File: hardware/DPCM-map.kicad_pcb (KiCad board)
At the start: 2 copper layers, 178 x 178 mm, 106 parts, among them J1 JMP, J10 Conn_01x03_Female, J2 Conn_01x06_Male, J3 Touch_Pad_+, J4 Touch_Pad_0, J5 Touch_Pad_-, J6 JMP, J7 Conn_01x06_Female, J8 Conn_01x03_Female, J9 Conn_01x03_Female, P1 USB_C_Plug, Q1 2N7002, Q2 2N7002, SW1 SW_Push, SW2 SW_+_Fb, SW3 SW_0_Fb, SW4 SW_-_Fb, U1 AZ1117-3.3, U2 BME280, U4 ESP32-WROOM-32, U5 CH340G, Y1 12MHz

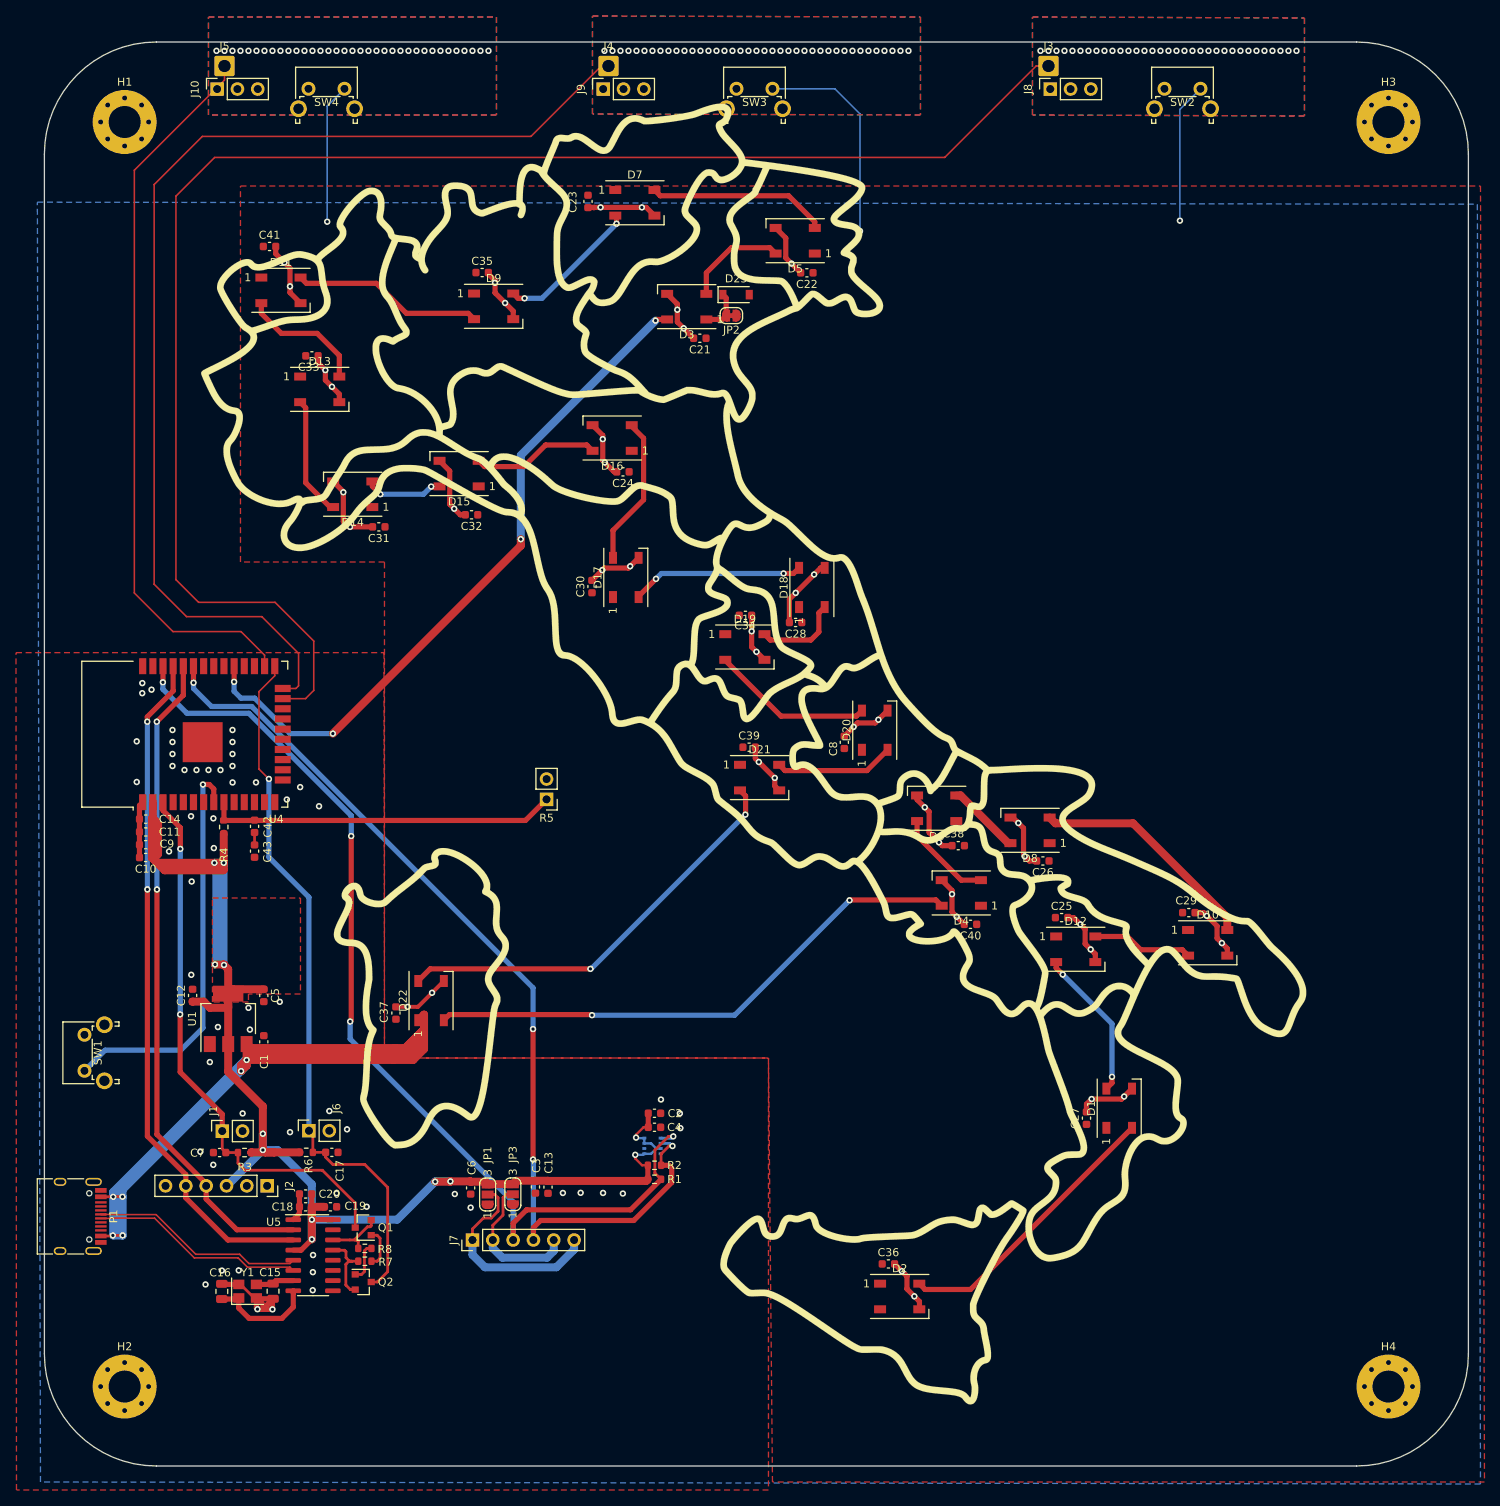
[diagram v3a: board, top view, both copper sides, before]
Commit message: route ws2813 mini and export
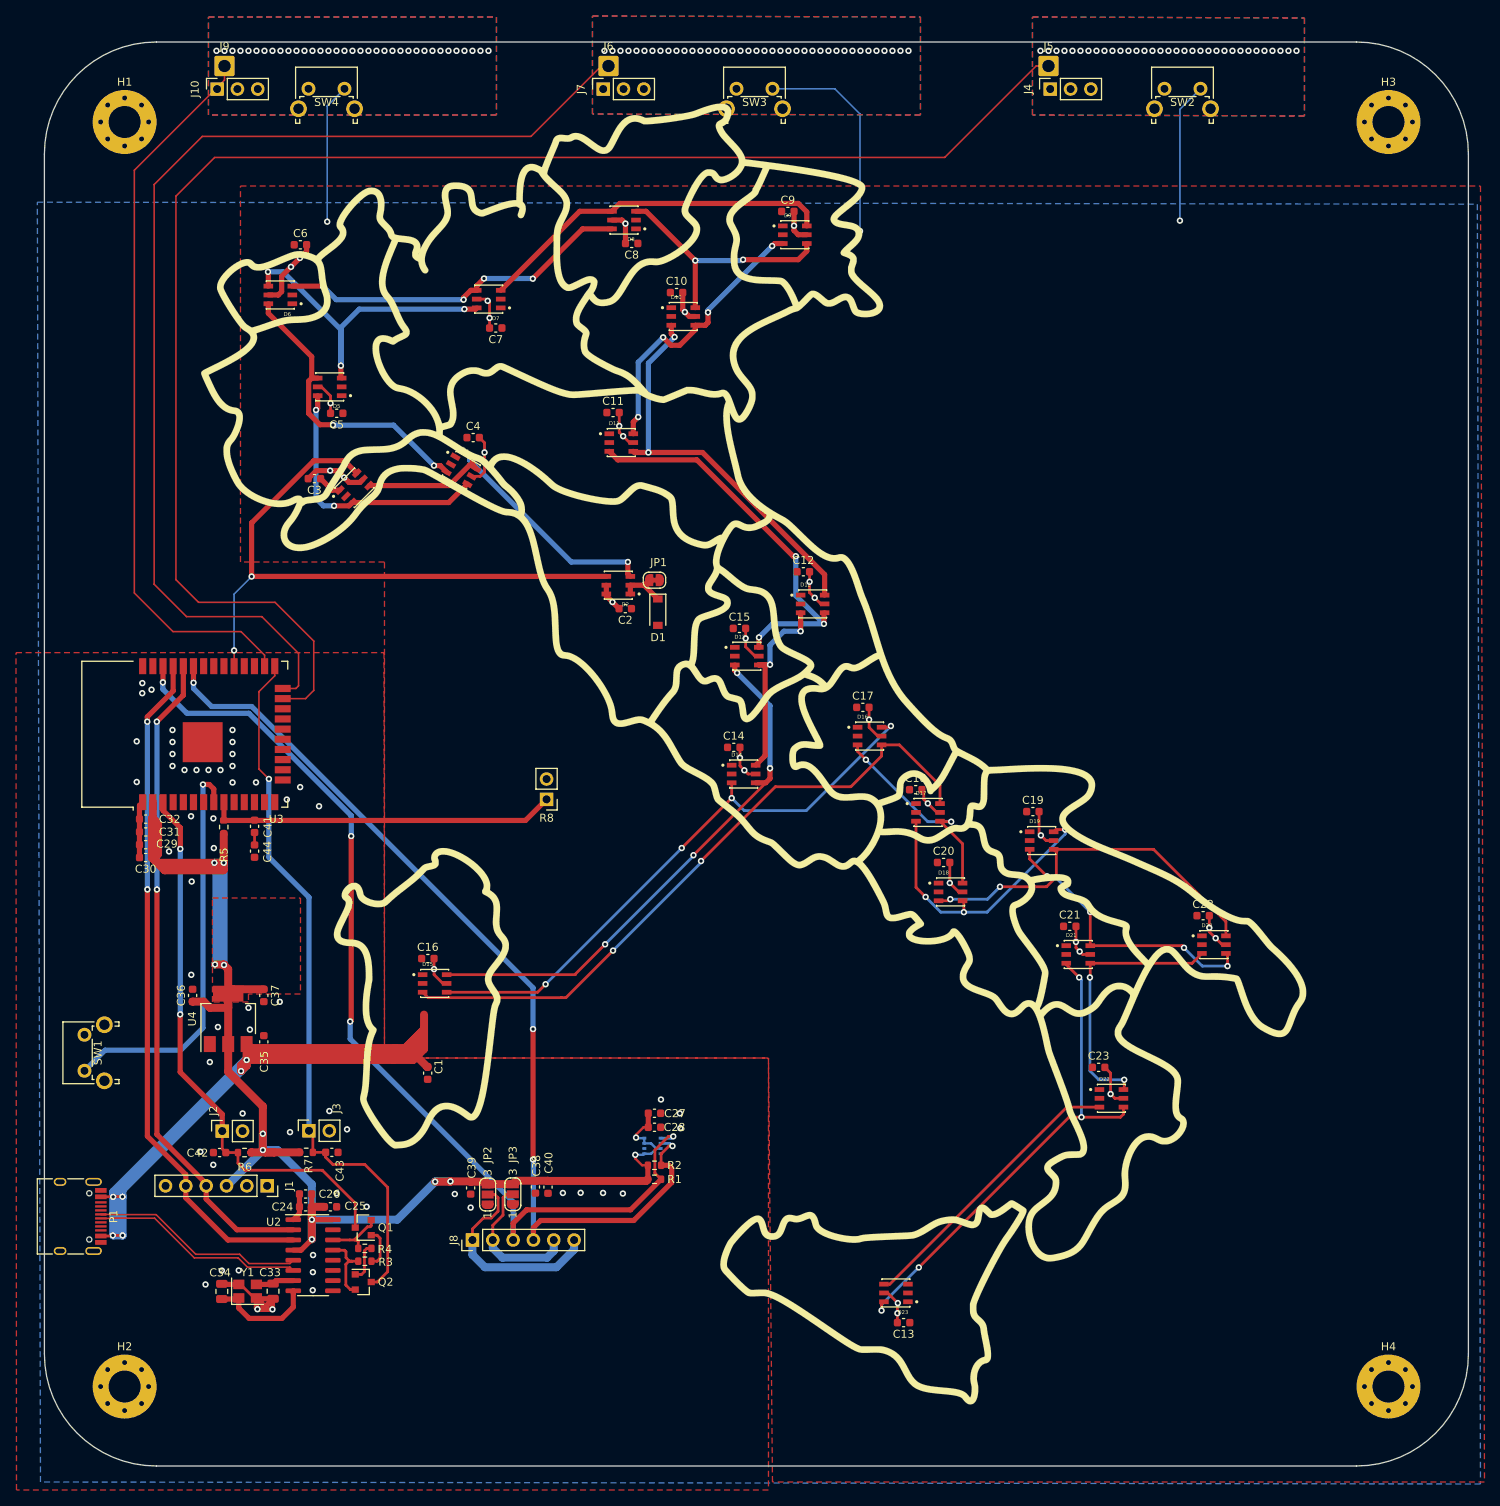
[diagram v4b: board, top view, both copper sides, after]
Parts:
- removed the C24 at (182.8, 103.7)
- removed the C25 at (237.6, 159.4)
- removed the C26 at (235.3, 152.4)
- removed the C27 at (240.8, 184.5)
- removed the C28 at (204.4, 122.6)
- removed the C29 at (253.5, 158.8)
- removed the C30 at (178.9, 118.1)
- removed the C31 at (152.3, 110.6)
- removed the C32 at (163.9, 109.1)
- removed the C33 at (143.9, 89.2)
- removed the C34 at (198.1, 121.7)
- removed the C35 at (165.2, 78.8)
- removed the C36 at (216.0, 202.7)
- removed the C37 at (154.4, 171.4)
- removed the C38 at (224.7, 150.5)
- removed the C39 at (198.6, 138.2)
- removed the C40 at (226.2, 160.3)
- removed the C41 at (138.6, 75.6)
- removed the JP2 at (196.4, 84.2)
- added C1: 10u, Capacitor_SMD:C_0603_1608Metric, F.Cu at (158.4, 178.9)
- added C10: 100n, Capacitor_SMD:C_0603_1608Metric, F.Cu at (189.5, 81.3)
- added C11: 100n, Capacitor_SMD:C_0603_1608Metric, F.Cu at (181.6, 96.3)
- added C12: 100n, Capacitor_SMD:C_0603_1608Metric, F.Cu at (205.4, 116.2)
- added C13: 100n, Capacitor_SMD:C_0603_1608Metric, F.Cu at (217.9, 210.1)
- added C14: 100n, Capacitor_SMD:C_0603_1608Metric, F.Cu at (196.7, 138.2)
- added C15: 100n, Capacitor_SMD:C_0603_1608Metric, F.Cu at (197.4, 123.3)
- added C16: 100n, Capacitor_SMD:C_0603_1608Metric, F.Cu at (158.4, 164.6)
- added C17: 100n, Capacitor_SMD:C_0603_1608Metric, F.Cu at (212.8, 133.2)
- added C18: 100n, Capacitor_SMD:C_0603_1608Metric, F.Cu at (219.4, 143.5)
- added C19: 100n, Capacitor_SMD:C_0603_1608Metric, F.Cu at (234.1, 146.2)
- added C2: 100n, Capacitor_SMD:C_0603_1608Metric, F.Cu at (183.1, 120.8)
- added C20: 100n, Capacitor_SMD:C_0603_1608Metric, F.Cu at (222.9, 152.6)
- added C3: 100n, Capacitor_SMD:C_0603_1608Metric, F.Cu at (144.2, 104.6)
- added C4: 100n, Capacitor_SMD:C_0603_1608Metric, F.Cu at (164.1, 99.5)
- added C5: 100n, Capacitor_SMD:C_0603_1608Metric, F.Cu at (147.0, 96.4)
- added C6: 100n, Capacitor_SMD:C_0603_1608Metric, F.Cu at (142.5, 75.3)
- added C7: 100n, Capacitor_SMD:C_0603_1608Metric, F.Cu at (166.9, 85.8)
- added C9: 100n, Capacitor_SMD:C_0603_1608Metric, F.Cu at (203.4, 71.2)
- added JP1: Jumper, Jumper:SolderJumper-2_P1.3mm_Bridged_RoundedPad1.0x1.5mm, F.Cu at (186.8, 117.3)
- C8: value 10u -> 100n
- D1: value WS2812B -> 1N4148W; footprint LED_SMD:LED_WS2812B_PLCC4_5.0x5.0mm_P3.2mm -> Diode_SMD:D_SOD-123
- D10, D11, D12, D13, D14, D15, D16, D17, D18, D19, D2, D20, D21, D22, D3, D4, D5, D6, D7, D8, D9: value WS2812B -> WS2813; footprint LED_SMD:LED_WS2812B_PLCC4_5.0x5.0mm_P3.2mm -> WS2813MINI:LED_WS2813-MINI
- D23: value 1N4148W -> WS2813; footprint Diode_SMD:D_SOD-123 -> WS2813MINI:LED_WS2813-MINI
- moved D23 126.4 mm to (216.9, 206.4), turned to 180 degrees
- moved C23 125.7 mm to (242.3, 178.2), turned to 0 degrees
- moved D6 104.2 mm to (140.0, 81.6)
- moved D10 102.1 mm to (190.3, 84.3)
- moved D2 95.6 mm to (182.2, 117.9), turned to 180 degrees
- moved C22 94.4 mm to (255.3, 159.2), turned to 0 degrees
- moved D8 91.6 mm to (182.9, 72.3)
- moved C21 86.8 mm to (238.7, 160.5), turned to 0 degrees
- moved D22 85.9 mm to (243.9, 182.0), turned to 0 degrees
- moved D1 84.7 mm to (187.2, 121.3), turned to 270 degrees
- moved D4 81.8 mm to (162.6, 103.5), turned to 330 degrees
- moved C8 67.8 mm to (183.9, 75.2), turned to 180 degrees
- moved D15 63.8 mm to (159.3, 167.7), turned to 0 degrees
- moved D13 62.9 mm to (198.3, 126.8)
- moved D5 61.0 mm to (146.2, 93.1)
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- renumbered C18 to C24, C19 to C25, C20 to C26, C2 to C27, C4 to C28, C9 to C29, C10 to C30, C11 to C31, C14 to C32, C15 to C33, C16 to C34, C1 to C35, C12 to C36, C5 to C37, C3 to C38, C6 to C39, C13 to C40, C42 to C41, C7 to C42, C17 to C43, C43 to C44, J2 to J1, J1 to J2, J6 to J3, J8 to J4, J3 to J5, J4 to J6, J9 to J7, J7 to J8, J5 to J9, JP1 to JP2, R7 to R3, R8 to R4, R4 to R5, R3 to R6, R6 to R7, R5 to R8, U2 to U1, U5 to U2, U4 to U3, U1 to U4
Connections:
- D1 pad 1: +5V -> Net-(D1-Pad1)
- D1 pad 2: Net-(D1-Pad2) -> +5V
- D10 pad 2: Net-(D10-Pad2) -> +5V
- D10 pad 3: GND -> Net-(D10-Pad3)
- D11 pad 2: Net-(D11-Pad2) -> +5V
- D11 pad 3: GND -> Net-(D11-Pad3)
- D11 pad 4: Net-(D11-Pad4) -> Net-(D10-Pad3)
- D12 pad 2: Net-(D1-Pad4) -> +5V
- D12 pad 3: GND -> Net-(D12-Pad3)
- D12 pad 4: Net-(D10-Pad2) -> Net-(D11-Pad3)
- D13 pad 2: Net-(D13-Pad2) -> +5V
- D13 pad 3: GND -> Net-(D13-Pad3)
- D13 pad 4: Net-(D11-Pad2) -> Net-(D12-Pad3)
- D14 pad 2: Net-(D14-Pad2) -> +5V
- D14 pad 3: GND -> Net-(D14-Pad3)
- D14 pad 4: Net-(D13-Pad2) -> Net-(D13-Pad3)
- D15 pad 2: Net-(D15-Pad2) -> +5V
- D15 pad 3: GND -> Net-(D15-Pad3)
- D15 pad 4: Net-(D14-Pad2) -> Net-(D14-Pad3)
- D16 pad 2: Net-(D16-Pad2) -> +5V
- D16 pad 3: GND -> Net-(D16-Pad3)
- D16 pad 4: Net-(D15-Pad2) -> Net-(D15-Pad3)
- D17 pad 2: Net-(D17-Pad2) -> +5V
- D17 pad 3: GND -> Net-(D17-Pad3)
- D17 pad 4: Net-(D16-Pad2) -> Net-(D16-Pad3)
- D18 pad 2: Net-(D18-Pad2) -> +5V
- D18 pad 3: GND -> Net-(D18-Pad3)
- D18 pad 4: Net-(D17-Pad2) -> Net-(D17-Pad3)
- D19 pad 2: Net-(D19-Pad2) -> +5V
- D19 pad 3: GND -> Net-(D19-Pad3)
- D19 pad 4: Net-(D18-Pad2) -> Net-(D18-Pad3)
- D2 pad 1: +5V -> Net-(D1-Pad1)
- D2 pad 2: (no net) -> Net-(D1-Pad1)
- D2 pad 3: GND -> Net-(D2-Pad3)
- D2 pad 4: Net-(D1-Pad2) -> LED_CHAIN
- D20 pad 2: Net-(D20-Pad2) -> +5V
- D20 pad 3: GND -> Net-(D20-Pad3)
- D20 pad 4: Net-(D19-Pad2) -> Net-(D19-Pad3)
- D21 pad 2: Net-(D21-Pad2) -> +5V
- D21 pad 3: GND -> Net-(D21-Pad3)
- D21 pad 4: Net-(D20-Pad2) -> Net-(D20-Pad3)
- D22 pad 2: Net-(D22-Pad2) -> +5V
- D22 pad 3: GND -> Net-(D22-Pad3)
- D22 pad 4: Net-(D21-Pad2) -> Net-(D21-Pad3)
- D23 pad 1: Net-(D23-Pad1) -> +5V
- D3 pad 1: Net-(D23-Pad1) -> +5V
- D3 pad 2: Net-(D3-Pad2) -> +5V
- D3 pad 3: GND -> Net-(D3-Pad3)
- D3 pad 4: LED_CHAIN -> Net-(D2-Pad3)
- D4 pad 2: Net-(D4-Pad2) -> +5V
- D4 pad 3: GND -> Net-(D4-Pad3)
- D4 pad 4: Net-(D22-Pad2) -> Net-(D3-Pad3)
- D5 pad 2: Net-(D5-Pad2) -> +5V
- D5 pad 3: GND -> Net-(D5-Pad3)
- D5 pad 4: Net-(D3-Pad2) -> Net-(D4-Pad3)
- D6 pad 2: Net-(D6-Pad2) -> +5V
- D6 pad 3: GND -> Net-(D6-Pad3)
- D6 pad 4: Net-(D4-Pad2) -> Net-(D5-Pad3)
- D7 pad 2: Net-(D7-Pad2) -> +5V
- D7 pad 3: GND -> Net-(D7-Pad3)
- D7 pad 4: Net-(D5-Pad2) -> Net-(D6-Pad3)
- D8 pad 2: Net-(D10-Pad4) -> +5V
- D8 pad 3: GND -> Net-(D10-Pad6)
- D8 pad 4: Net-(D6-Pad2) -> Net-(D7-Pad3)
- D9 pad 2: Net-(D11-Pad4) -> +5V
- D9 pad 3: GND -> Net-(D10-Pad4)
- D9 pad 4: Net-(D7-Pad2) -> Net-(D10-Pad6)
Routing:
- net Net-(D15-Pad3): track 0.00 -> 83.3 mm, vias 0 -> 2
- net Net-(D14-Pad3): track 0.00 -> 73.8 mm, vias 0 -> 4
- net Net-(D13-Pad3): track 0.00 -> 70.0 mm, vias 0 -> 4
- net Net-(D22-Pad2): track 68.8 -> 0.00 mm, vias 2 -> 0
- net Net-(D21-Pad3): track 0.00 -> 63.0 mm, vias 0 -> 4
- net GND: track 259.2 -> 203.2 mm, vias 103 -> 93
- net Net-(D21-Pad2): track 52.9 -> 0.00 mm, vias 2 -> 0
- net Net-(D10-Pad3): track 0.00 -> 50.3 mm, vias 0 -> 2
- net Net-(D11-Pad3): track 0.00 -> 50.2 mm, vias 0 -> 3
- net Net-(D18-Pad3): track 0.00 -> 46.6 mm, vias 0 -> 2
- net Net-(D7-Pad3): track 0.00 -> 44.9 mm
- net Net-(D6-Pad3): track 0.00 -> 44.8 mm, vias 0 -> 4
- net Net-(D2-Pad3): track 0.00 -> 43.4 mm, vias 0 -> 2
- net Net-(D5-Pad3): track 0.00 -> 42.8 mm, vias 0 -> 3
- net Net-(D4-Pad3): track 0.00 -> 37.1 mm, vias 0 -> 2
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
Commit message: Added production files
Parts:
- added G***: LOGO, map_edges_keepout:vulcano, F.Cu at (227.0, 189.0)
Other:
- board text added: "JLCJLCJLCJLC"
